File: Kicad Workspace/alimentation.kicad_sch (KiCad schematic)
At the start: 23 parts, among them U6 TLV76733DRVx, U7 LM5017MR, U8 LT3042xMSE

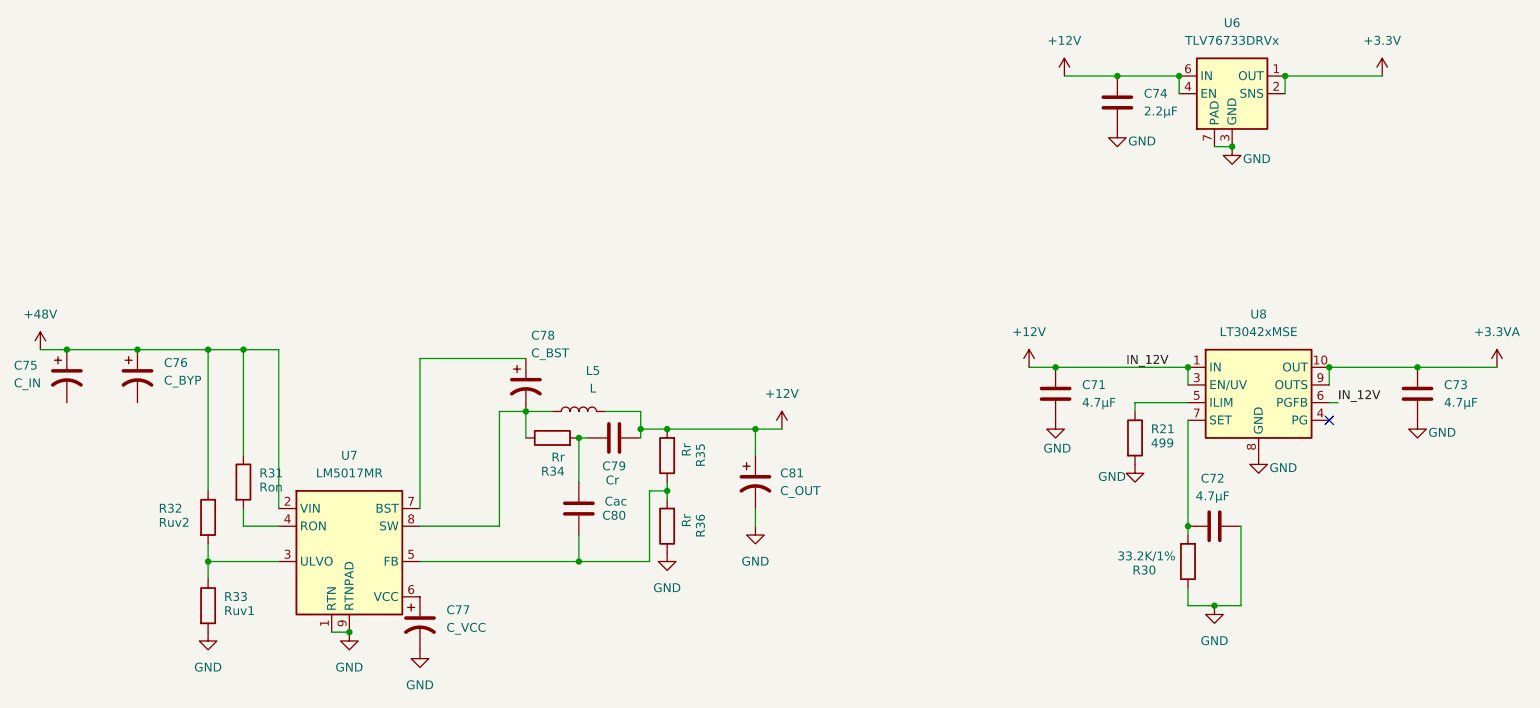
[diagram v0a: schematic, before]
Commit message: feat: alim stage done + adapt to 36V input voltage instead of 48
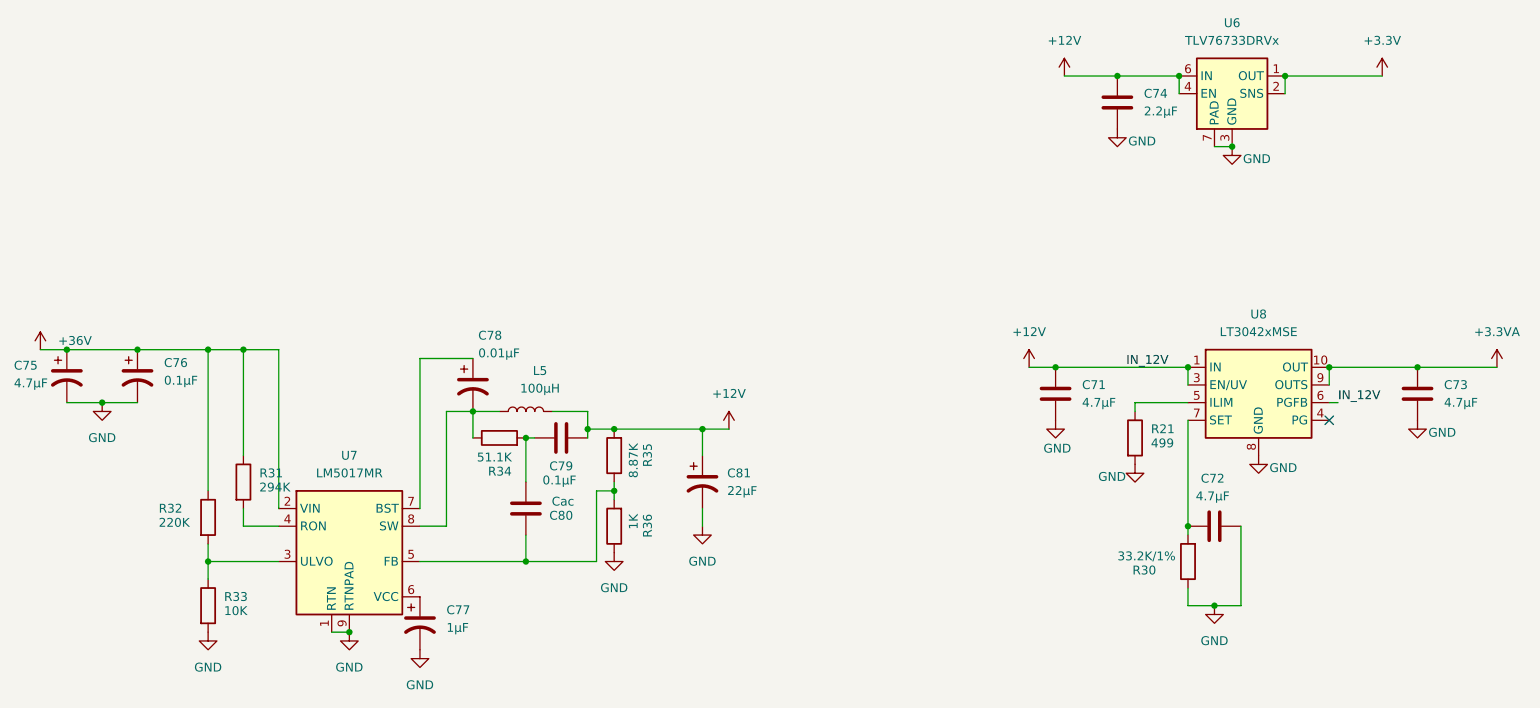
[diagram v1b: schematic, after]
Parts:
- C75: value C_IN -> 4.7µF
- C76: value C_BYP -> 0.1µF
- C77: value C_VCC -> 1µF
- C78: value C_BST -> 0.01µF
- C79: value Cr -> 0.1µF
- C81: value C_OUT -> 22µF
- L5: value L -> 100µH
- R31: value Ron -> 294K
- R32: value Ruv2 -> 220K
- R33: value Ruv1 -> 10K
- R34: value Rr -> 51.1K
- R35: value Rr -> 8.87K
- R36: value Rr -> 1K
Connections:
- net GND: now also C75.2, C76.2
- net +48V renamed +36V
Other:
- moved on the sheet: C78, C79, C80, C81, L5, R34, R35, R36

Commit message: feat: correction work in progress
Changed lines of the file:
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@@
 	(wire
 		(pts
-			(xy 223.52 93.98) (xy 222.25 93.98)
+			(xy 222.25 93.98) (xy 226.06 93.98)
 		)
 		(stroke
@@
 		)
 	)
-	(label "IN_12V"
-		(at 193.04 88.9 0)
-		(effects
-			(font
-				(size 1.27 1.27)
-			)
-			(justify left bottom)
-		)
-	)
-	(label "IN_12V"
-		(at 223.52 93.98 0)
-		(effects
-			(font
-				(size 1.27 1.27)
-			)
-			(justify left bottom)
-		)
-	)
-	(label ""
-		(at 195.58 88.9 0)
-		(effects
-			(font
-				(size 1.27 1.27)
-			)
-			(justify left bottom)
-		)
-	)
 	(symbol
 		(lib_id "Device:R")
@@
 					(unit 1)
 				)
+			)
+		)
+	)
+	(symbol
+		(lib_id "power:+12V")
+		(at 226.06 93.98 0)
+		(unit 1)
+		(body_style 1)
+		(exclude_from_sim no)
+		(in_bom yes)
+		(on_board yes)
+		(in_pos_files yes)
+		(dnp no)
+		(property "Reference" "#PWR078"
+			(at 226.06 97.79 0)
+			(hide yes)
+			(show_name no)
+			(do_not_autoplace no)
+			(effects
+				(font
+					(size 1.27 1.27)
+				)
+			)
+		)
+		(property "Value" "+12V"
+			(at 227.838 95.25 0)
+			(show_name no)
+			(do_not_autoplace no)
+			(effects
+				(font
+					(size 1.27 1.27)
+				)
+			)
+		)
+		(property "Footprint" ""
+			(at 226.06 93.98 0)
+			(hide yes)
+			(show_name no)
+			(do_not_autoplace no)
+			(effects
+				(font
+					(size 1.27 1.27)
+				)
+			)
+		)
+		(property "Datasheet" ""
+			(at 226.06 93.98 0)
+			(hide yes)
+			(show_name no)
+			(do_not_autoplace no)
+			(effects
+				(font
+					(size 1.27 1.27)
+				)
+			)
+		)
+		(property "Description" "Power symbol creates a global label with name \"+12V\""
+			(at 226.06 93.98 0)
+			(hide yes)
+			(show_name no)
+			(do_not_autoplace no)
+			(effects
+				(font
+					(size 1.27 1.27)
+				)
+			)
+		)
+		(pin "1"
+		)
+		(instances
+			(project "Kicad Workspace"
+				(path "/7c7afbb1-f4ab-42aa-9bad-41afd809eff4/d3077e0a-2bdd-4420-a49c-97d03fd12563"
+					(reference "#PWR078")
+					(unit 1)
+				)

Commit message: feat: routing work in progress
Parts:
- C71, C72, C73: footprint (none) -> Capacitor_SMD:C_0805_2012Metric
- C74: footprint (none) -> Capacitor_SMD:C_0201_0603Metric
- R21, R34: footprint (none) -> Resistor_SMD:R_0201_0603Metric
- R30: footprint (none) -> Resistor_SMD:R_0805_2012Metric
- R31, R32, R33, R35, R36: footprint (none) -> Resistor_SMD:R_01005_0402Metric
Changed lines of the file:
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@@
 			)
 		)
-		(property "Footprint" ""
+		(property "Footprint" "Resistor_SMD:R_01005_0402Metric"
 			(at 121.158 111.76 90)
 			(hide yes)
@@
 			)
 		)
-		(property "Footprint" ""
+		(property "Footprint" "Resistor_SMD:R_01005_0402Metric"
 			(at 59.182 110.49 90)
 			(hide yes)
@@
 			)
 		)
-		(property "Footprint" ""
+		(property "Footprint" "Resistor_SMD:R_0201_0603Metric"
 			(at 102.87 100.838 90)
 			(hide yes)
@@
 			)
 		)
-		(property "Footprint" ""
+		(property "Footprint" "Capacitor_SMD:C_0805_2012Metric"
 			(at 235.9152 96.52 0)
 			(hide yes)
@@
 			)
 		)
-		(property "Footprint" ""
+		(property "Footprint" "Resistor_SMD:R_01005_0402Metric"
 			(at 59.182 123.19 90)
 			(hide yes)
@@
 			)
 		)
-		(property "Footprint" ""
+		(property "Footprint" "Resistor_SMD:R_0201_0603Metric"
 			(at 192.532 99.06 90)
 			(hide yes)
@@
 			)
 		)
-		(property "Footprint" ""
+		(property "Footprint" "Capacitor_SMD:C_0805_2012Metric"
 			(at 183.8452 96.52 0)
 			(hide yes)
@@
 			)
 		)
-		(property "Footprint" ""
+		(property "Footprint" "Capacitor_SMD:C_0201_0603Metric"
 			(at 192.7352 54.61 0)
 			(hide yes)
@@
 			)
 		)
-		(property "Footprint" ""
+		(property "Footprint" "Resistor_SMD:R_01005_0402Metric"
 			(at 121.158 101.6 90)
 			(hide yes)
@@
 			)
 		)
-		(property "Footprint" ""
+		(property "Footprint" "Capacitor_SMD:C_0805_2012Metric"
 			(at 209.55 110.7948 0)
 			(hide yes)
@@
 			)
 		)
-		(property "Footprint" ""
+		(property "Footprint" "Resistor_SMD:R_01005_0402Metric"
 			(at 64.262 105.41 90)
 			(hide yes)
@@
 			)
 		)
-		(property "Footprint" ""
+		(property "Footprint" "Resistor_SMD:R_0805_2012Metric"
 			(at 203.708 116.84 90)
 			(hide yes)
